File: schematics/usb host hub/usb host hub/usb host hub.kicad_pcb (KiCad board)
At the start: 2 copper layers, 129 x 37.1 mm, 48 parts, among them J1 USB_A, J2 USB_A, J3 USB_A, J4 Conn_01x04_Male, J5 532610671, U1 RP2040, U2 FE1.1s, U3 W25Q128JVS, U4 AZ1117EH-3.3TRG1, U5 USBLC6-2SC6, U6 USBLC6-2SC6, U7 USBLC6-2SC6, Y1 12MHz, Y2 12MHz

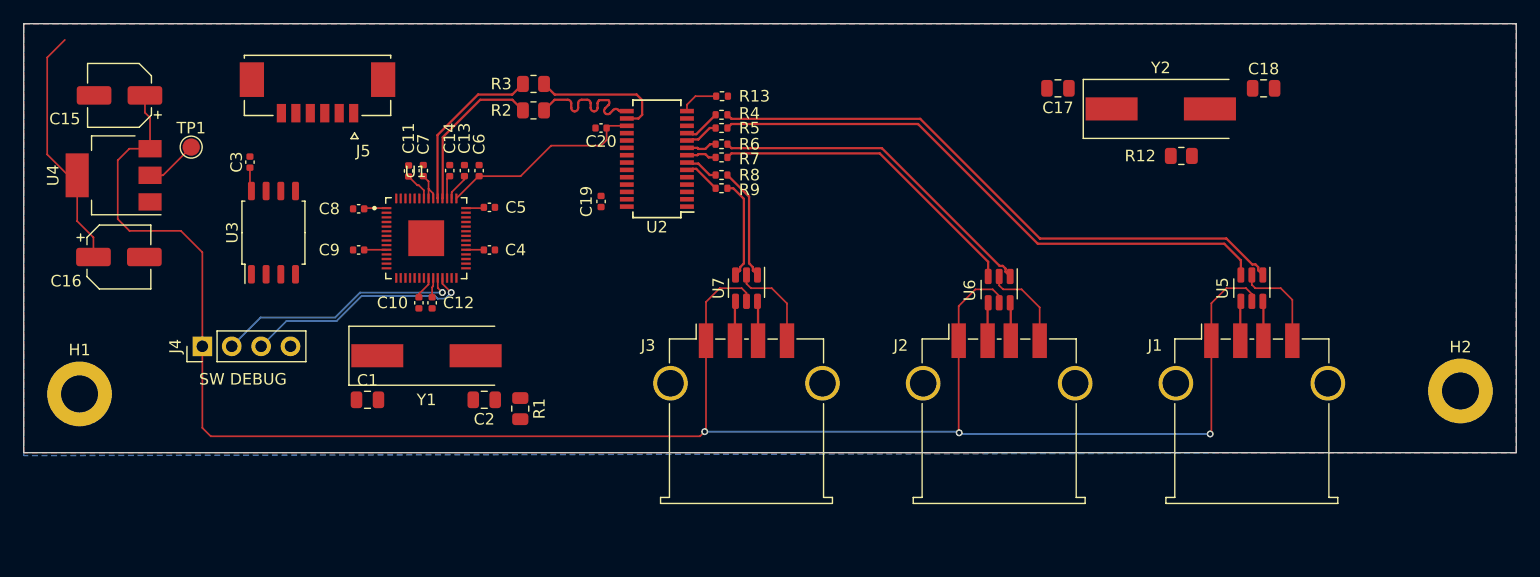
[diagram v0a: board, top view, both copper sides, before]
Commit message: Rv32: USB host schematic updated.
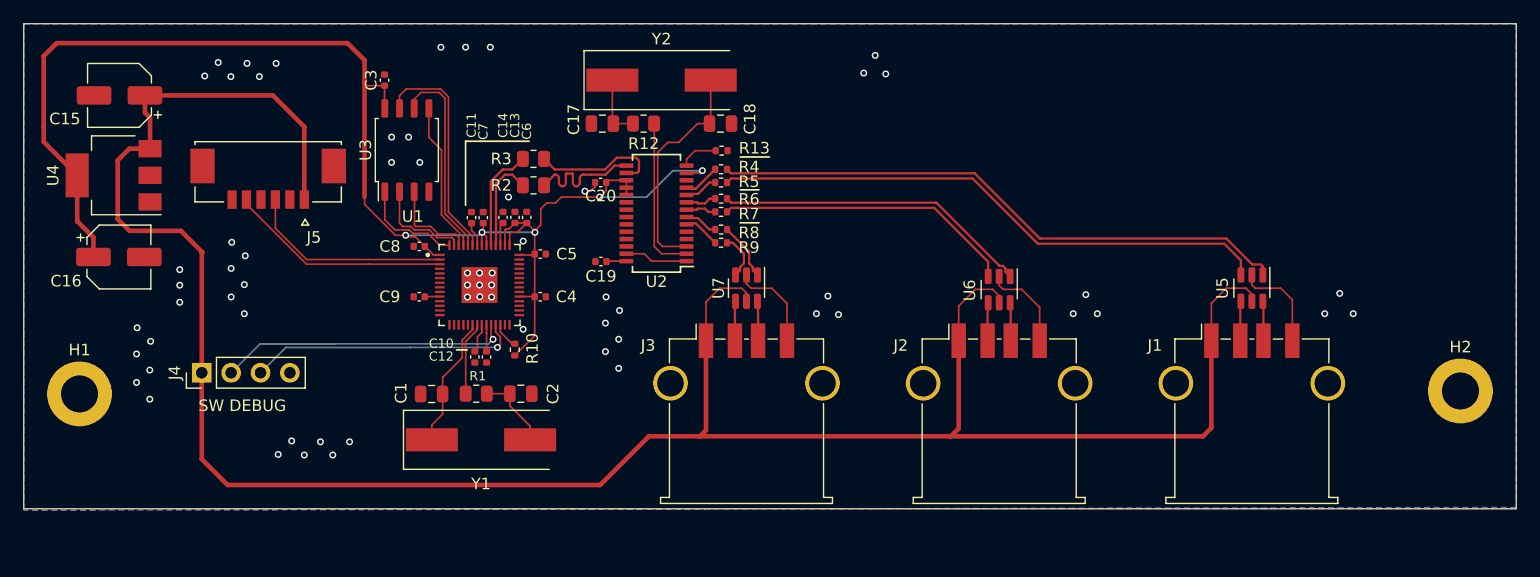
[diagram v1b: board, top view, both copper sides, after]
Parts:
- removed TP1: TestPoint, TestPoint:TestPoint_Pad_D1.5mm
- added R10: 10k, Resistor_SMD:R_0402_1005Metric, F.Cu at (92.0, 84.3)
- moved C18 47.1 mm to (109.8, 64.8)
- moved R12 46.6 mm to (103.1, 64.8)
- moved Y2 43.2 mm to (104.7, 61.0)
- moved C17 39.5 mm to (99.6, 64.8)
- moved C3 13.6 mm to (80.7, 61.0)
- moved U3 13.6 mm to (82.7, 67.1)
- moved Y1 8.67 mm to (89.1, 92.1)
- moved J5 8.60 mm to (70.7, 68.9)
- moved C11 6.77 mm to (88.2, 72.9)
- moved C10 6.73 mm to (88.5, 84.9)
- moved C12 6.64 mm to (89.5, 84.9)
- moved C9 6.61 mm to (83.7, 79.7)
- moved C7 6.59 mm to (89.3, 72.9)
- moved R2 6.48 mm to (93.6, 70.1)
- moved R3 6.48 mm to (93.6, 67.8)
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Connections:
- J5 pad 3: UART_RX -> UART_TX
- J5 pad 5: UART_TX -> UART_RX
- U1 pad 19: unconnected-(U1-Pad19) -> GND
- U1 pad 26: unconnected-(U1-Pad26) -> RUN
- U2 pad 18: unconnected-(U2-Pad18) -> +3V3
- U2 pad 19: unconnected-(U2-Pad19) -> +3V3
- U2 pad 26: unconnected-(U2-Pad26) -> +3V3
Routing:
- net +3V3: track 60.6 -> 135.9 mm, vias 0 -> 5
- net VBUS: track 172.7 -> 199.8 mm, vias 3 -> 0
- net QSPI_SD3: track 0.00 -> 19.8 mm
- net Net-(C18-Pad1): track 0.00 -> 19.7 mm
- net UART_RX: track 0.00 -> 19.3 mm
- net UART_TX: track 0.00 -> 17.8 mm
- net QSPI_SCLK: track 0.00 -> 17.4 mm
- net Net-(R12-Pad2): track 0.00 -> 13.7 mm
- net QSPI_SD0: track 0.00 -> 13.5 mm
- net XIN: track 0.00 -> 11.4 mm
- net QSPI_CSN: track 0.00 -> 8.92 mm
- net QSPI_SD1: track 0.00 -> 8.52 mm
- net QSPI_SD2: track 0.00 -> 7.86 mm
- net GND: track 24.5 -> 31.4 mm, vias 0 -> 65
- net Net-(C2-Pad1): track 0.00 -> 6.71 mm
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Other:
- board size 129 x 37.1 mm -> 129 x 41.9 mm

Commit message: Rv32: Some work on USB HID board.
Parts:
- J5: value 532610671 -> Conn_01x04_Male; footprint 532610671:MOLEX_532610671 -> Connector_JST:JST_EH_B4B-EH-A_1x04_P2.50mm_Vertical
- moved J5 3.32 mm to (73.9, 69.6)
- moved J4 1.47 mm to (66.4, 86.3)
- moved C12 0.57 mm to (89.6, 84.4)
- moved C10 0.57 mm to (88.5, 84.4)
- moved R10 0.55 mm to (91.4, 84.4)
- moved C16 0.26 mm to (57.8, 76.0)
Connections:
- net Net-(C19-Pad1) renamed /VD18
- J4 pad 2: SWCLK -> SWD
- J4 pad 3: SWD -> SWCLK
- J5 pad 1: VBUS -> GND
- J5 pad 2: GND -> UART_TX
- J5 pad 3: UART_TX -> UART_RX
- J5 pad 4: GND -> VBUS
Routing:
- net SWD: track 23.6 -> 53.2 mm, vias 1 -> 0
- net SWCLK: track 25.2 -> 52.2 mm, vias 1 -> 0
- net +3V3: track 135.9 -> 162.1 mm, vias 5 -> 7
- net VBUS: track 199.8 -> 175.0 mm
- net /VD18: track 1.74 -> 12.2 mm, vias 0 -> 2
- net GND: track 31.4 -> 33.5 mm, vias 65 -> 73
- net UART_TX: track 17.8 -> 19.4 mm
- net UART_RX: track 19.3 -> 20.9 mm
- net +1V1: track 6.12 -> 7.11 mm, vias 0 -> 1
- net QSPI_SD2: track 7.86 -> 6.94 mm
- net QSPI_SD1: track 8.52 -> 7.82 mm
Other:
- board text added: "USB HID Connector Board - Rev 1 Anders Pistol"
- board text added: "VBUS"

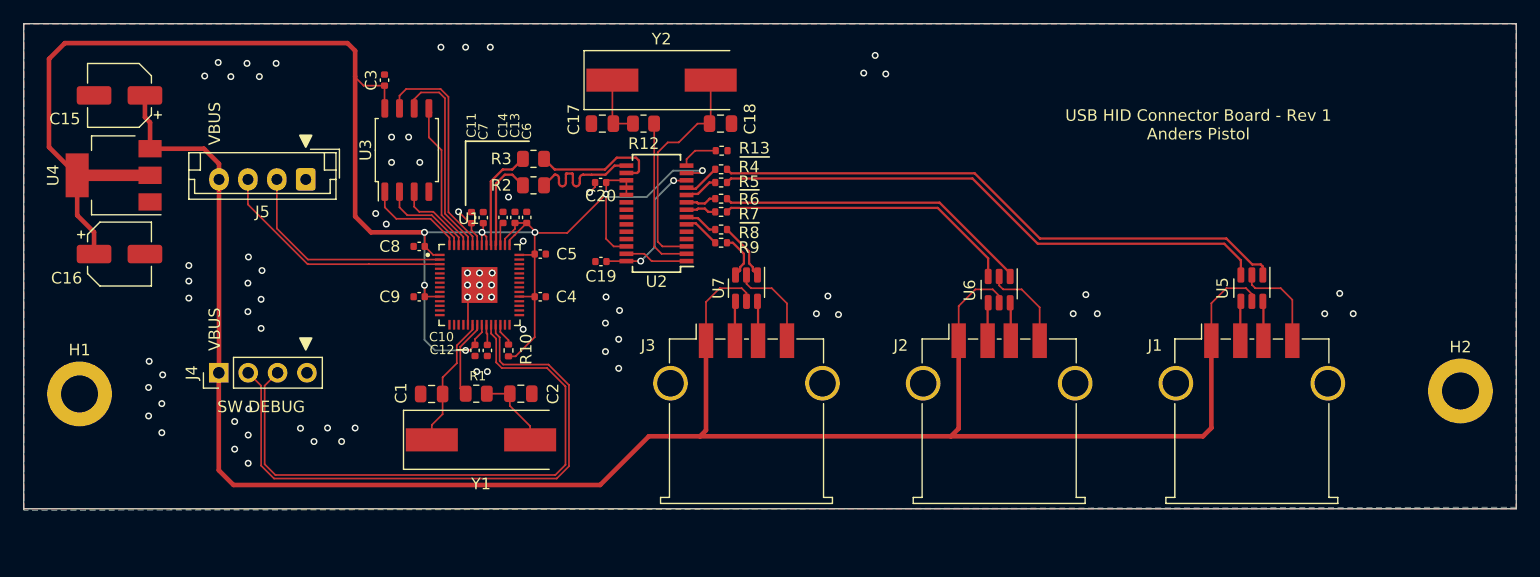
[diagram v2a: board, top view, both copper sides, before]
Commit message: Rv32: More USB host board work, using USB connector available on JLCPCB.
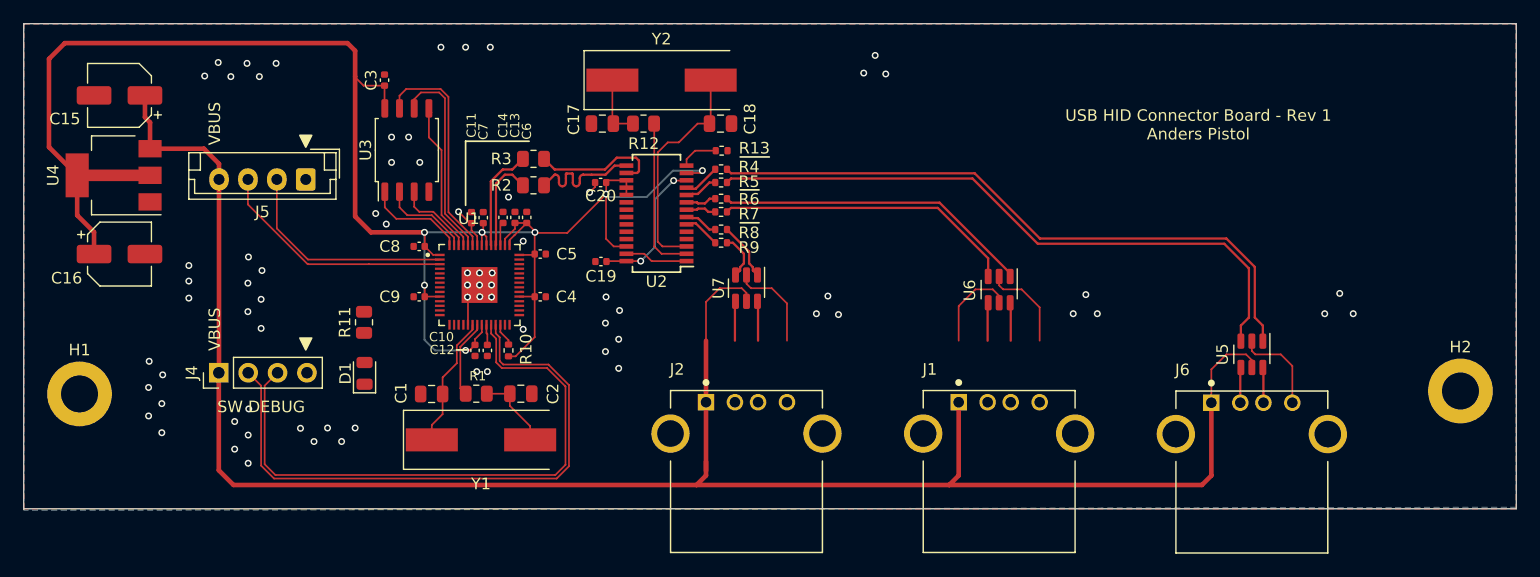
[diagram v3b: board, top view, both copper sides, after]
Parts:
- removed J3: USB_A, Connector_USB:USB_A_TE_292303-7_Horizontal
- added D1: LED, LED_SMD:LED_0805_2012Metric, F.Cu at (79.0, 86.4)
- added J6: 292303-1, 292303-1:TE_292303-1, F.Cu at (152.2, 88.9)
- added R11: 1k, Resistor_SMD:R_0805_2012Metric, F.Cu at (78.9, 82.0)
- J1, J2: value USB_A -> 292303-1; footprint Connector_USB:USB_A_TE_292303-7_Horizontal -> 292303-1:TE_292303-1
- moved J2 25.4 mm to (108.5, 88.9)
- moved J1 25.4 mm to (130.4, 88.9)
- moved U5 5.72 mm to (155.7, 84.7)
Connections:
- J1 pad 2: ESD_USB_D1- -> ESD_USB_D2-
- J1 pad 3: ESD_USB_D1+ -> ESD_USB_D2+
- J2 pad 2: ESD_USB_D2- -> ESD_USB_D3-
- J2 pad 3: ESD_USB_D2+ -> ESD_USB_D3+
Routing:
- net USB_D1-: track 48.8 -> 55.1 mm
- net USB_D1+: track 50.5 -> 55.8 mm
- net VBUS: track 175.0 -> 175.8 mm

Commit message: Rv32: USB HID HUB schematic updated. Ordered from JLCPCB.
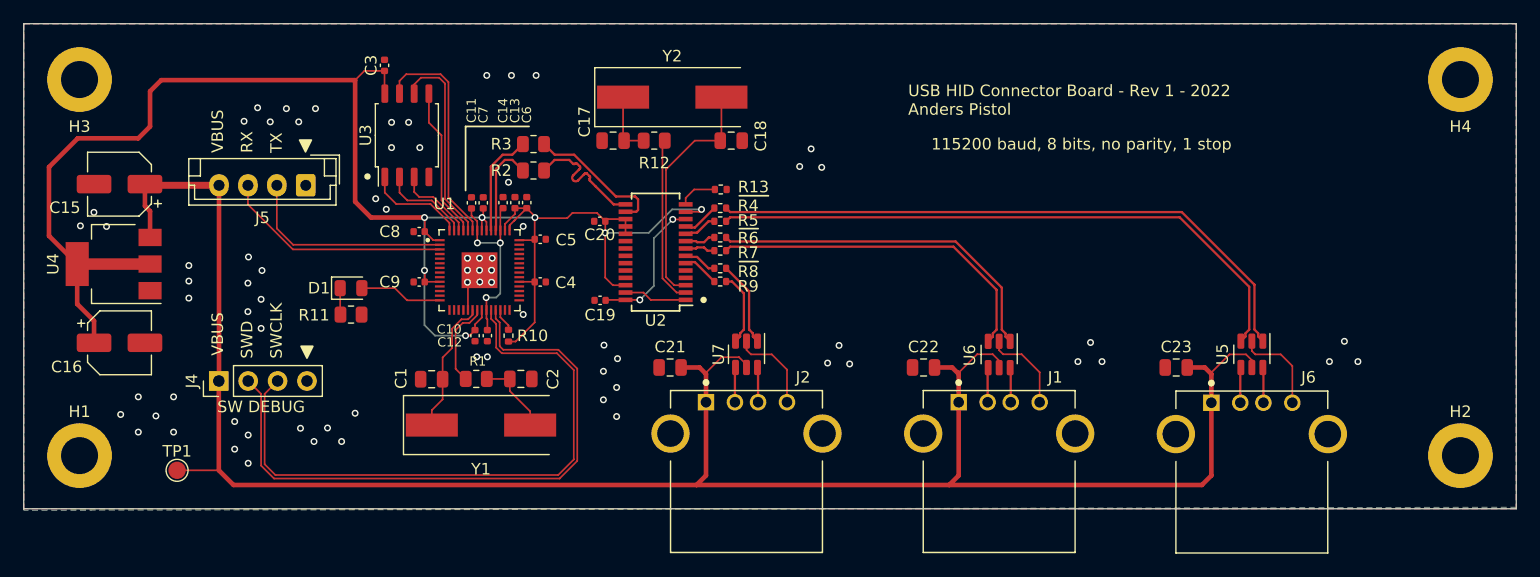
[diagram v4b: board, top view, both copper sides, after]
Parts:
- added C21: 10uF, Capacitor_SMD:C_0805_2012Metric, F.Cu at (105.4, 85.9)
- added C22: 10uF, Capacitor_SMD:C_0805_2012Metric, F.Cu at (127.3, 85.9)
- added C23: 10uF, Capacitor_SMD:C_0805_2012Metric, F.Cu at (149.2, 85.9)
- added H3: MountingHole, MountingHole:MountingHole_3.2mm_M3_DIN965_Pad, F.Cu at (54.4, 61.0)
- added H4: MountingHole, MountingHole:MountingHole_3.2mm_M3_DIN965_Pad, F.Cu at (173.7, 61.0)
- added TP1: TestPoint_Small, TestPoint:TestPoint_Pad_D1.5mm, F.Cu at (62.8, 94.7)
- R11: value 1k -> 33
- moved C16 7.67 mm to (57.8, 83.7)
- moved U4 7.67 mm to (57.3, 76.9)
- moved C15 7.67 mm to (57.8, 70.0)
- moved D1 7.46 mm to (77.8, 79.0), turned to 0 degrees
- moved U7 5.72 mm to (112.0, 84.7)
- moved U6 5.61 mm to (133.9, 84.7)
- moved H2 5.59 mm to (173.7, 93.5)
- moved H1 5.33 mm to (54.4, 93.5)
- moved C19 3.35 mm to (99.4, 80.0)
- moved C20 3.35 mm to (99.3, 73.2)
- moved R13 3.35 mm to (109.8, 70.5)
- moved R4 3.35 mm to (109.7, 72.1)
- moved R5 3.35 mm to (109.7, 73.2)
- moved R6 3.35 mm to (109.7, 74.6)
- moved R7 3.35 mm to (109.7, 75.8)
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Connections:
- U1 pad 14: unconnected-(U1-Pad14) -> STATUS_LED
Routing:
- net +1V1: track 7.11 -> 16.5 mm, vias 1 -> 3
- net VBUS: track 175.8 -> 184.8 mm
- net STATUS_LED: track 0.00 -> 7.17 mm
- net USB_D2-: track 26.1 -> 29.8 mm
- net USB_D2+: track 27.4 -> 30.6 mm
- net +3V3: track 162.1 -> 159.4 mm
- net USB_D3-: track 3.99 -> 6.39 mm
- net USB_D3+: track 5.02 -> 7.42 mm
- net Net-(D1-Pad1): track 0.00 -> 2.30 mm
- net USB_D1+: track 55.8 -> 53.6 mm
- net USB_D1-: track 55.1 -> 52.9 mm
- net SWD: track 53.2 -> 55.0 mm
- net SWCLK: track 52.2 -> 54.0 mm
- net Net-(C18-Pad1): track 19.7 -> 20.8 mm
- net GND: track 33.1 -> 32.1 mm, vias 73 -> 74
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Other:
- board text added: "115200 baud, 8 bits, no parity, 1 stop"
- board text added: "RX"
- board text added: "SWCLK"
- board text added: "SWD"
- board text added: "TX"
- board text added: "USB HID Connector Board - Rev 1 - 2022 Anders Pistol"
- board text removed: "USB HID Connector Board - Rev 1 Anders Pistol"

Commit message: Rv32: Rev 2 USB Host schematics. Ordered from JLCPCB.
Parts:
- removed C18: 27pF, Capacitor_SMD:C_0805_2012Metric
- added R14: 33k, Resistor_SMD:R_0805_2012Metric, F.Cu at (142.2, 86.0)
- added R15: 33k, Resistor_SMD:R_0805_2012Metric, F.Cu at (120.2, 86.0)
- added TP_1V1: TestPoint_Small, TestPoint:TestPoint_Pad_D1.5mm, F.Cu at (88.7, 60.4)
- added TP_DRV1: TestPoint_Small, TestPoint:TestPoint_Pad_D1.5mm, F.Cu at (101.0, 92.5)
- added TP_LED1: TestPoint_Small, TestPoint:TestPoint_Pad_D1.5mm, F.Cu at (101.0, 88.9)
- added TP_LED2: TestPoint_Small, TestPoint:TestPoint_Pad_D1.5mm, F.Cu at (101.0, 85.4)
- C17: value 27pF -> 100nF; footprint Capacitor_SMD:C_0805_2012Metric -> Capacitor_SMD:C_0402_1005Metric
- R11: value 33 -> 47
- R12: value 1k -> 33k
- moved R12 63.1 mm to (164.1, 85.8)
- moved C19 14.1 mm to (106.2, 67.7), turned to 0 degrees
- moved C17 11.6 mm to (99.4, 77.7)
- moved C20 11.5 mm to (109.8, 68.5), turned to 0 degrees
- moved R13 3.16 mm to (109.8, 67.3)
- moved R4 2.25 mm to (109.8, 69.8)
- moved R5 2.25 mm to (109.8, 71.0)
- moved R6 2.25 mm to (109.8, 72.4)
- moved R7 2.25 mm to (109.8, 73.5)
- moved R8 2.25 mm to (109.8, 75.0)
- moved R9 2.25 mm to (109.8, 76.2)
- moved U2 2.25 mm to (104.2, 73.6)
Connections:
- C17 pad 1: Net-(C17-Pad1) -> /VD18
- J1 pad SH1: unconnected-(J1-PadSH1) -> Net-(J1-PadSH1)
- J1 pad SH2: unconnected-(J1-PadSH1) -> Net-(J1-PadSH1)
- J2 pad SH1: unconnected-(J2-PadSH1) -> Net-(J2-PadSH1)
- J2 pad SH2: unconnected-(J2-PadSH1) -> Net-(J2-PadSH1)
- J6 pad SH1: unconnected-(J6-PadSH1) -> Net-(J6-PadSH1)
- J6 pad SH2: unconnected-(J6-PadSH1) -> Net-(J6-PadSH1)
- R12 pad 1: Net-(C17-Pad1) -> Net-(J6-PadSH1)
- R12 pad 2: Net-(R12-Pad2) -> GND
- U2 pad 2: Net-(R12-Pad2) -> Net-(Y2-Pad1)
- U2 pad 22: unconnected-(U2-Pad22) -> /DRV
- U2 pad 23: unconnected-(U2-Pad23) -> /LED1
- U2 pad 24: unconnected-(U2-Pad24) -> /LED2
- U2 pad 27: GND -> unconnected-(U2-Pad27)
- Y2 pad 1: Net-(C17-Pad1) -> Net-(Y2-Pad1)
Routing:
- net /DRV: track 0.00 -> 22.9 mm, vias 0 -> 2
- net Net-(Y2-Pad1): track 0.00 -> 18.5 mm
- net /LED1: track 0.00 -> 18.2 mm, vias 0 -> 2
- net Net-(R12-Pad2): track 14.5 -> 0.00 mm
- net /LED2: track 0.00 -> 13.8 mm, vias 0 -> 2
- net +1V1: track 16.5 -> 29.4 mm
- net Net-(J6-PadSH1): track 0.00 -> 6.24 mm
- net Net-(J1-PadSH1): track 0.00 -> 5.92 mm
- net Net-(J2-PadSH1): track 0.00 -> 5.88 mm
- net Net-(C17-Pad1): track 5.49 -> 0.00 mm
- net GND: track 32.1 -> 26.6 mm, vias 74 -> 88
- net +3V3: track 159.4 -> 163.8 mm
- net /VD18: track 12.2 -> 15.6 mm
- net USB_D3-: track 6.39 -> 8.64 mm
- net USB_D1-: track 52.9 -> 55.1 mm
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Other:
- outline, holes or cut-outs redrawn
- board text added: "USB HID Connector Board - Rev 2 - 2022 Anders Pistol"
- board text removed: "115200 baud, 8 bits, no parity, 1 stop"
- board text removed: "USB HID Connector Board - Rev 1 - 2022 Anders Pistol"
